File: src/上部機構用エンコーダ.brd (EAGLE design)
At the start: 15 parts

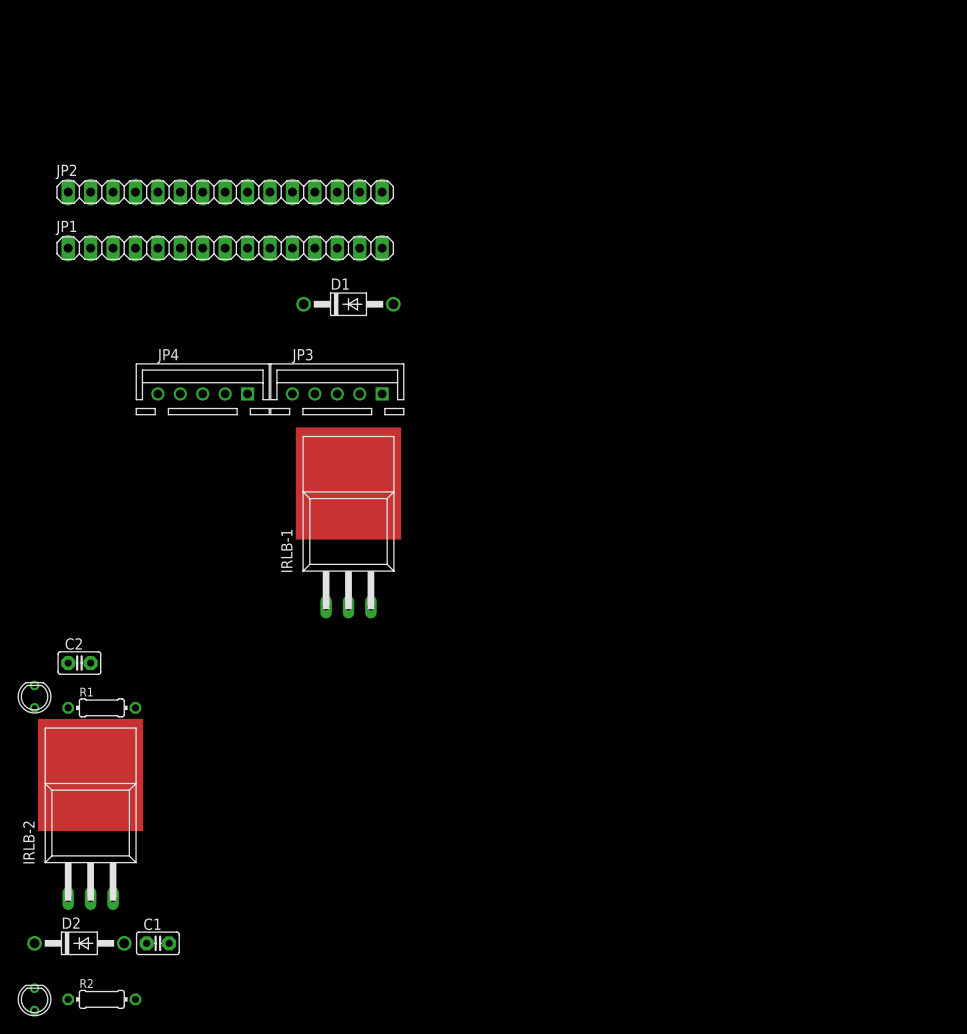
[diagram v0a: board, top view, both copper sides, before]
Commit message: 上部機構用エンコーダー 回路の微修正
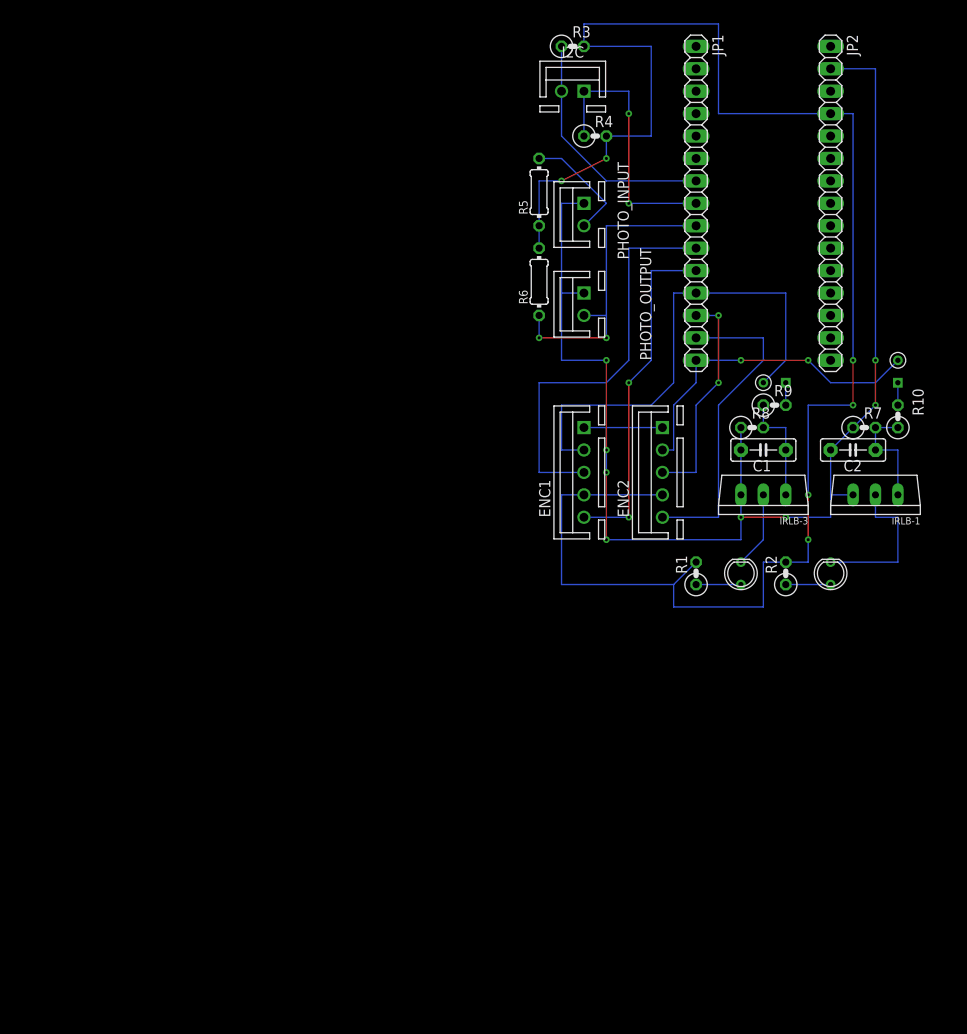
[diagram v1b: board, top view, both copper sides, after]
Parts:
- removed IRLB-2: IRLB3813_2, OKUDA_libraries:TO-220AB-PUT
- removed JP3, JP4: (no value), con-jst-xh:B5B-XH
- added ENC1, ENC2: (no value), con-jst-xh:B5B-XH
- added I2C, PHOTO_INPUT, PHOTO_OUTPUT: 02-JST, con-jst-xh:B2B-XH
- added IRLB-3: IRLB3813STAND, OKUDA_libraries:TO-220AB-STAND
- added R10, R9: 10, rcl:0207/2V
- added R3, R4: 2.2k, rcl:0207/2V
- added R5: 100, rcl:0204/7
- added R6: 10k, rcl:0204/7
- added R7, R8: 100k, rcl:0207/2V
- C1, C2: device capacitor-wima:C2.5-2 -> capacitor-wima:C5B2.5
- D1, D2: value 1N4942 -> DIODE_STAND; device diode:DO41-10 -> DIODE_STAND:DIODE_STAND
- IRLB-1: value IRLB3813_2 -> IRLB3813STAND; device OKUDA_libraries:TO-220AB-PUT -> OKUDA_libraries:TO-220AB-STAND
- R1, R2: value (none) -> 330; device rcl:0204/7 -> rcl:0207/2V
- moved D2 112.4 mm to (43.2, 27.9), turned to 270 degrees
- moved U$3 102.3 mm to (35.6, 5.08)
- moved R2 91.3 mm to (30.5, 6.35), turned to 90 degrees
- moved C2 90.9 mm to (38.1, 20.3), turned to 180 degrees
- moved C1 88.5 mm to (27.9, 20.3), turned to 180 degrees
- moved U$2 81.2 mm to (25.4, 5.08)
- moved R1 69.0 mm to (20.3, 6.35), turned to 90 degrees
- moved JP2 68.6 mm to (35.6, 48.3), turned to 270 degrees
- moved IRLB-1 60.2 mm to (40.6, 15.2), turned to 180 degrees
- moved JP1 53.6 mm to (20.3, 48.3), turned to 270 degrees
- moved D1 50.3 mm to (30.5, 27.9)
- moved U$1 44.4 mm to (45.7, 0.00), turned to 90 degrees
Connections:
- new net N$7: PHOTO_INPUT.2, R5.2
- new net N$8: D1.C, R9.2
- new net N$9: D2.C, R10.2
- new net PHOTO_OUT: JP1.9, PHOTO_OUTPUT.2, R6.1
- new net SCL: I2C.1, JP1.8, R4.1
- new net SDA: I2C.2, JP1.7, R3.1
- net 5V: now also ENC1.4, ENC2.4, R3.2, R4.2, R5.1, R6.2; no longer JP3.4, JP4.4
- net ENC1_A: now also ENC1.3; no longer JP3.3
- net ENC1_B: now also ENC1.5; no longer JP3.5
- net ENC1_X: now also ENC1.2; no longer JP3.2
- net ENC2_A: now also ENC2.3; no longer JP4.3
- net ENC2_B: now also ENC2.5; no longer JP4.5
- net ENC2_X: now also ENC2.2; no longer JP4.2
- net GND: now also ENC1.1, ENC2.1, IRLB-3.S, PHOTO_INPUT.1, PHOTO_OUTPUT.1, R7.1, R8.1; no longer IRLB-2.S, JP3.1, JP4.1
- net N$1: now also IRLB-3.D; no longer IRLB-1.P$1
- net N$3: now also C1.1, IRLB-3.G, R8.2, R9.1; no longer C2.1, D1.C, IRLB-1.G
- net N$4: now also C2.1, IRLB-1.G, R10.1, R7.2; no longer C1.1, D2.C, IRLB-2.G
- net N$5: now also IRLB-1.D; no longer IRLB-2.P$1
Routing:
- net 5V: track 0.00 -> 201.0 mm, vias 0 -> 6
- net GND: track 0.00 -> 158.3 mm, vias 0 -> 8
- net ENC1_X: track 0.00 -> 55.4 mm
- net ENC1_A: track 0.00 -> 46.8 mm
- net ENC1_B: track 0.00 -> 39.2 mm, vias 0 -> 2
- net ENC2_X: track 0.00 -> 37.4 mm, vias 0 -> 2
- net ENC2_B: track 0.00 -> 36.4 mm
- net PHOTO_OUT: track 0.00 -> 35.6 mm, vias 0 -> 2
- net SCL: track 0.00 -> 30.5 mm, vias 0 -> 2
- net SDA: track 0.00 -> 27.5 mm
- net ENC2_A: track 0.00 -> 25.2 mm, vias 0 -> 2
- net N$5: track 0.00 -> 17.8 mm
- net N$7: track 0.00 -> 13.3 mm
- net N$4: track 0.00 -> 12.7 mm
- net N$3: track 0.00 -> 12.7 mm
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
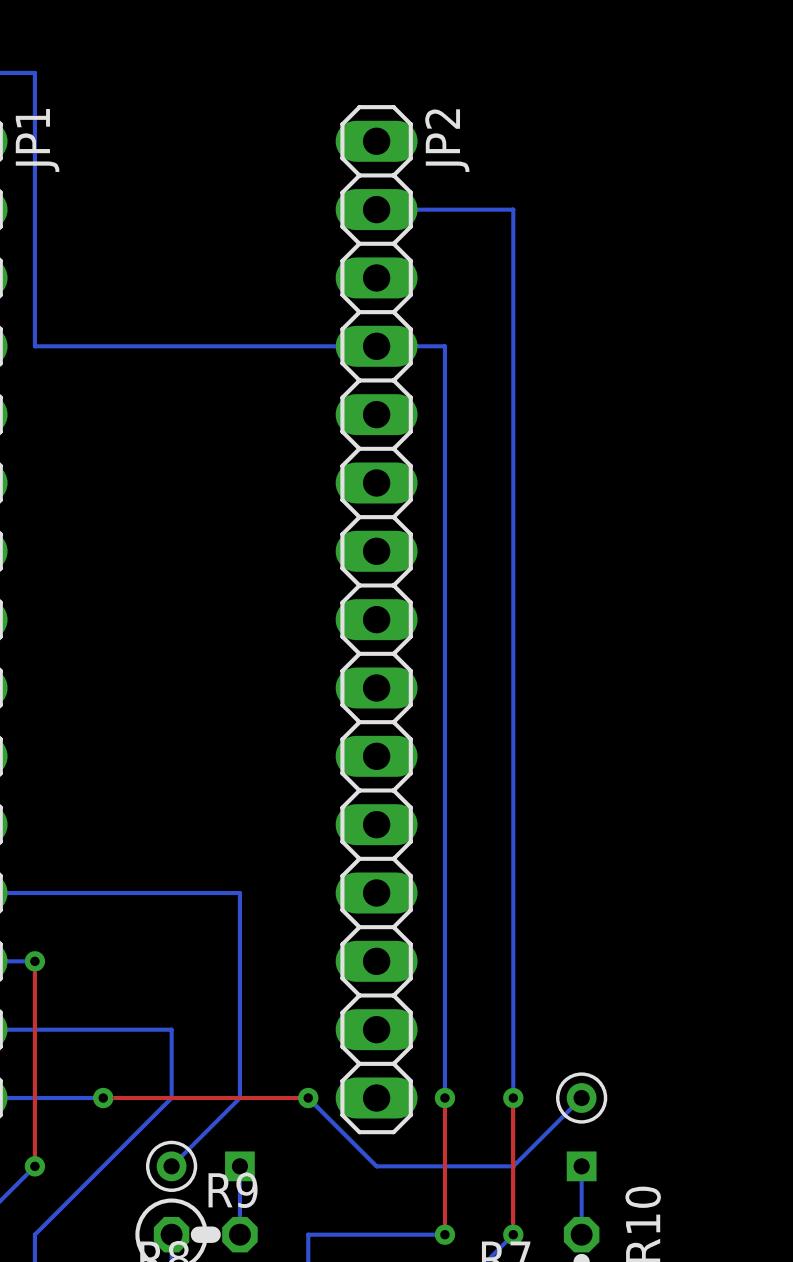
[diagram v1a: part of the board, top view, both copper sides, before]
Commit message: 国技館コントローラの追加
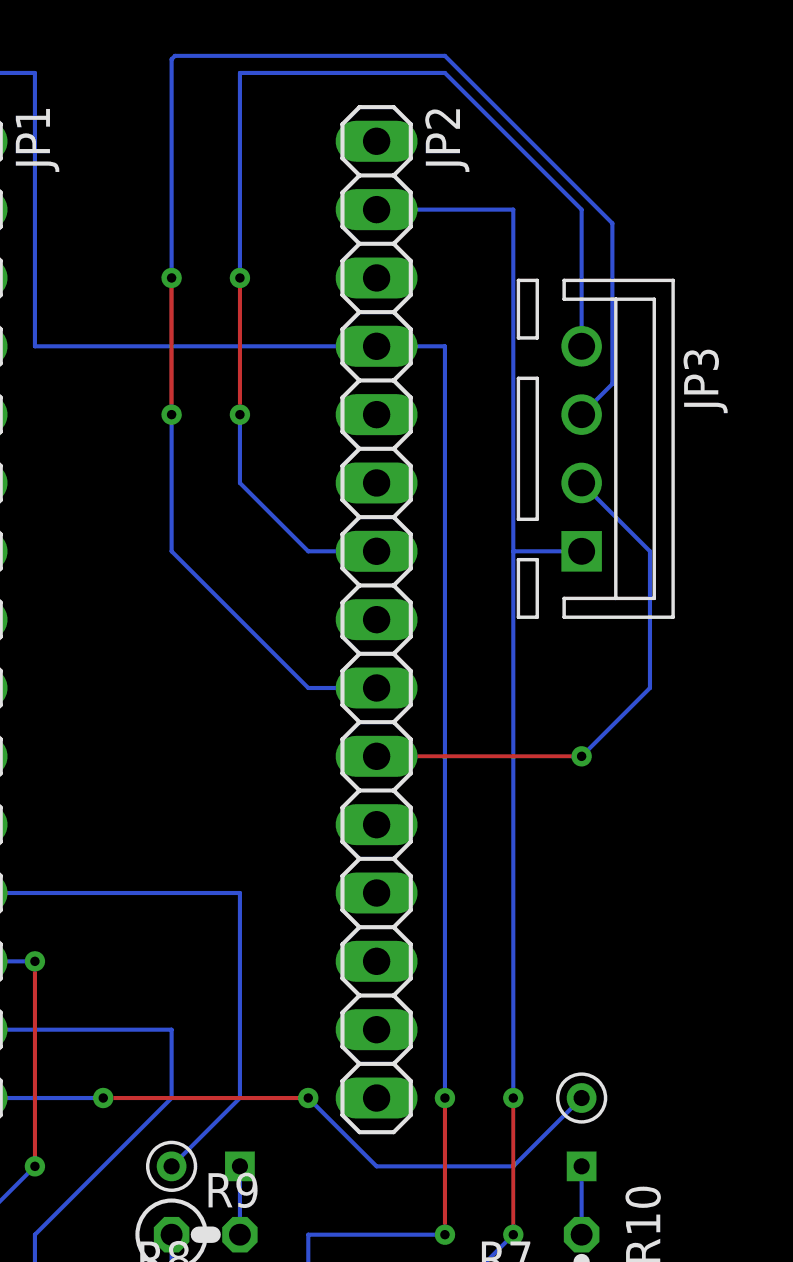
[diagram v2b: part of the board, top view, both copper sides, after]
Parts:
- added JP3: (no value), con-jst-xh:B4B-XH
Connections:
- new net BLUE: JP2.10, JP3.2
- new net GREEN: JP2.9, JP3.3
- new net RED: JP2.7, JP3.4
- net GND: now also JP3.1
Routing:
- net GREEN: track 0.00 -> 54.6 mm, vias 0 -> 2
- net RED: track 0.00 -> 41.3 mm, vias 0 -> 2
- net BLUE: track 0.00 -> 19.9 mm, vias 0 -> 1
- net GND: track 158.3 -> 160.9 mm
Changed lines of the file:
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@@
 <element name="D1" library="DIODE_STAND" package="DIODE_STAND" value="DIODE_STAND" x="30.48" y="27.94" smashed="yes"/>
 <element name="D2" library="DIODE_STAND" package="DIODE_STAND" value="DIODE_STAND" x="43.18" y="27.94" smashed="yes" rot="R270"/>
+<element name="JP3" library="con-jst-xh" package="B4B-XH" value="" x="43.18" y="54.61" smashed="yes" rot="R270">
+<attribute name="NAME" x="46.99" y="58.42" size="1.27" layer="25" rot="R270"/>
+<attribute name="VALUE" x="39.37" y="58.42" size="1.27" layer="27" rot="R270"/>
+</element>
 </elements>
 <signals>
@@
 <wire x1="35.56" y1="20.32" x2="38.1" y2="22.86" width="0.1524" layer="16"/>
 <wire x1="35.56" y1="63.5" x2="40.64" y2="63.5" width="0.1524" layer="16"/>
-<wire x1="40.64" y1="63.5" x2="40.64" y2="30.48" width="0.1524" layer="16"/>
+<wire x1="40.64" y1="63.5" x2="40.64" y2="50.8" width="0.1524" layer="16"/>
 <via x="40.64" y="30.48" extent="1-16" drill="0.35"/>
+<wire x1="40.64" y1="50.8" x2="40.64" y2="30.48" width="0.1524" layer="16"/>
 <wire x1="40.64" y1="30.48" x2="40.64" y2="25.4" width="0.1524" layer="1"/>
 <via x="40.64" y="25.4" extent="1-16" drill="0.35"/>
@@
 <wire x1="38.1" y1="22.86" x2="40.64" y2="25.4" width="0.1524" layer="16"/>
 <wire x1="10.16" y1="10.16" x2="25.4" y2="10.16" width="0.1524" layer="16"/>
+<contactref element="JP3" pad="1"/>
+<wire x1="43.18" y1="50.8" x2="40.64" y2="50.8" width="0.1524" layer="16"/>
 </signal>
 <signal name="5V">
@@
 <wire x1="43.18" y1="25.4" x2="43.18" y2="27.94" width="0.1524" layer="16"/>
 </signal>
+<signal name="BLUE">
+<contactref element="JP2" pad="10"/>
+<wire x1="35.56" y1="43.18" x2="43.18" y2="43.18" width="0.1524" layer="1"/>
+<via x="43.18" y="43.18" extent="1-16" drill="0.35"/>
+<contactref element="JP3" pad="2"/>
+<wire x1="43.18" y1="53.34" x2="45.72" y2="50.8" width="0.1524" layer="16"/>
+<wire x1="45.72" y1="50.8" x2="45.72" y2="45.72" width="0.1524" layer="16"/>
+<wire x1="45.72" y1="45.72" x2="43.18" y2="43.18" width="0.1524" layer="16"/>
+</signal>
+<signal name="GREEN">
+<contactref element="JP2" pad="9"/>
+<contactref element="JP3" pad="3"/>
+<wire x1="43.18" y1="55.88" x2="44.323" y2="57.023" width="0.1524" layer="16"/>
+<wire x1="44.323" y1="57.023" x2="44.323" y2="62.992" width="0.1524" layer="16"/>
+<wire x1="44.323" y1="62.992" x2="38.1" y2="69.215" width="0.1524" layer="16"/>
+<wire x1="38.1" y1="69.215" x2="28.067" y2="69.215" width="0.1524" layer="16"/>
+<wire x1="28.067" y1="69.215" x2="27.94" y2="69.088" width="0.1524" layer="16"/>
+<wire x1="27.94" y1="69.088" x2="27.94" y2="60.96" width="0.1524" layer="16"/>
+<via x="27.94" y="60.96" extent="1-16" drill="0.35"/>
+<wire x1="27.94" y1="60.96" x2="27.94" y2="55.88" width="0.1524" layer="1"/>
+<via x="27.94" y="55.88" extent="1-16" drill="0.35"/>
+<wire x1="27.94" y1="55.88" x2="27.94" y2="50.8" width="0.1524" layer="16"/>
+<wire x1="27.94" y1="50.8" x2="33.02" y2="45.72" width="0.1524" layer="16"/>
+<wire x1="33.02" y1="45.72" x2="35.56" y2="45.72" width="0.1524" layer="16"/>
+</signal>
+<signal name="RED">
+<contactref element="JP2" pad="7"/>
+<contactref element="JP3" pad="4"/>
+<wire x1="43.18" y1="58.42" x2="43.18" y2="63.5" width="0.1524" layer="16"/>
+<wire x1="43.18" y1="63.5" x2="38.1" y2="68.58" width="0.1524" layer="16"/>
+<wire x1="38.1" y1="68.58" x2="30.48" y2="68.58" width="0.1524" layer="16"/>
+<wire x1="30.48" y1="68.58" x2="30.48" y2="60.96" width="0.1524" layer="16"/>
+<via x="30.48" y="60.96" extent="1-16" drill="0.35"/>
+<wire x1="30.48" y1="60.96" x2="30.48" y2="55.88" width="0.1524" layer="1"/>
+<via x="30.48" y="55.88" extent="1-16" drill="0.35"/>
+<wire x1="30.48" y1="55.88" x2="30.48" y2="53.34" width="0.1524" layer="16"/>
+<wire x1="30.48" y1="53.34" x2="33.02" y2="50.8" width="0.1524" layer="16"/>
+<wire x1="33.02" y1="50.8" x2="35.56" y2="50.8" width="0.1524" layer="16"/>
+</signal>
 </signals>
